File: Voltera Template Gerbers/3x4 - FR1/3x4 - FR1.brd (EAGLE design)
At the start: 135 x 101.6 mm, 1 part

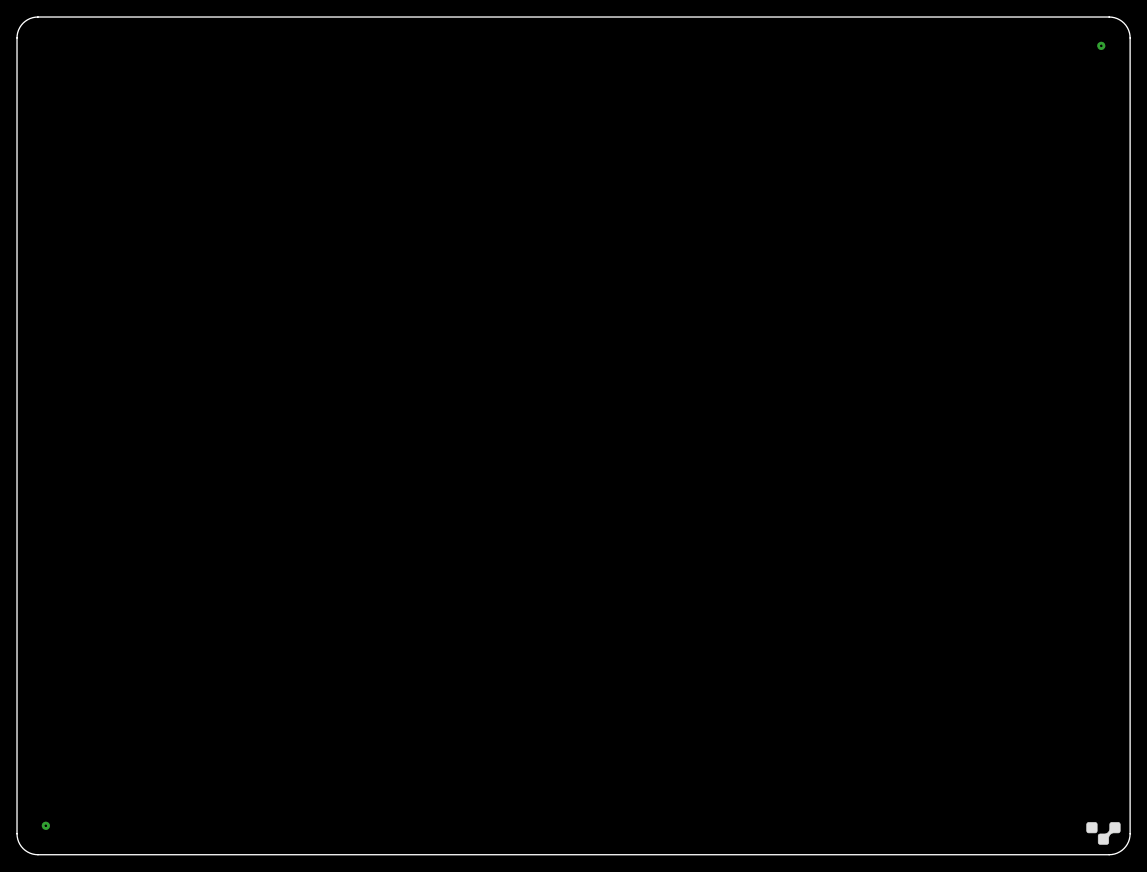
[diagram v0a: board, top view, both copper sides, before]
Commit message: Created 2x3 and 3x4 FR1 templates. Added 'fab' version of the templates
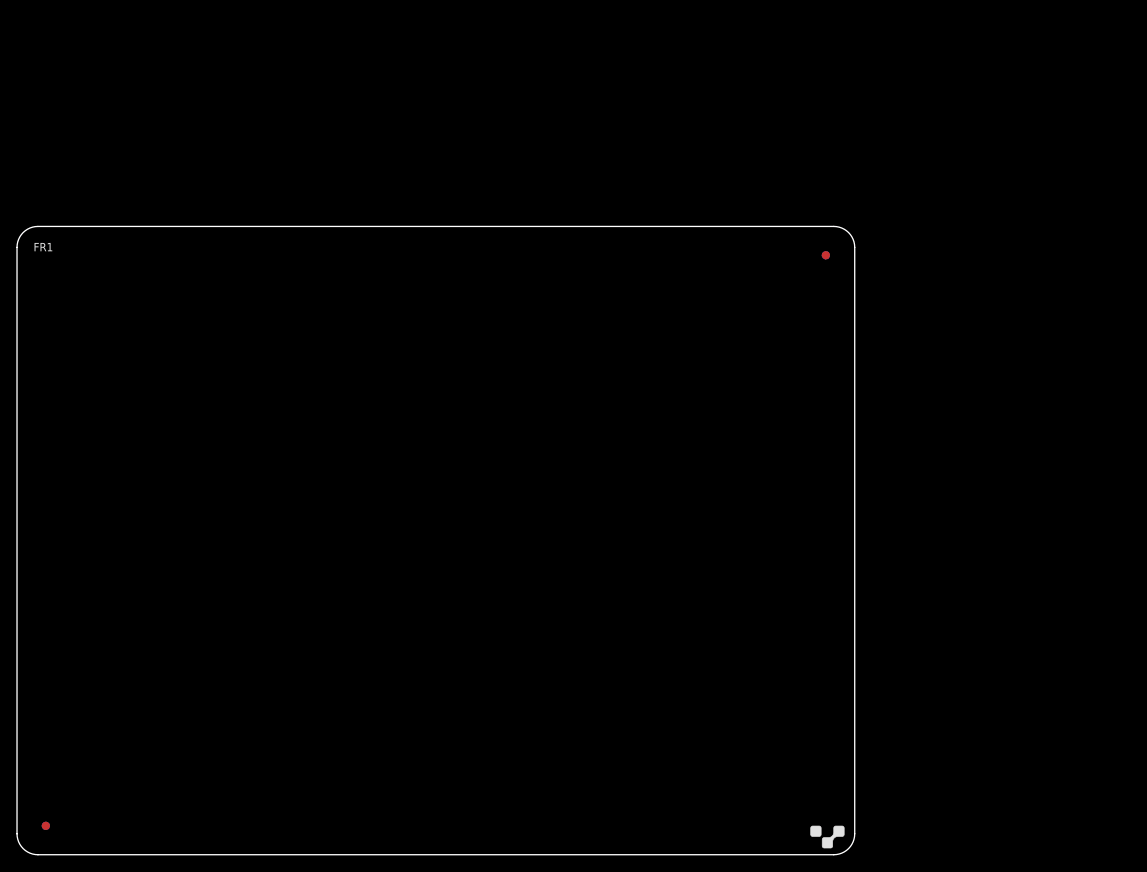
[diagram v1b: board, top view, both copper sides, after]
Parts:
- E$1: device voltera_community_lib:4X5_BOARD -> voltera_EAGLE_community_lib:3X4_BOARD_FR1
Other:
- board size 135 x 101.6 mm -> 101.6 x 76.2 mm
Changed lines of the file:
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@@
 <setting verticaltext="up"/>
 </settings>
-<grid distance="1" unitdist="mm" unit="mm" style="lines" multiple="1" display="yes" altdistance="0.1" altunitdist="mm" altunit="mm"/>
+<grid distance="0.05" unitdist="inch" unit="inch" style="lines" multiple="1" display="no" altdistance="0.025" altunitdist="inch" altunit="inch"/>
 <layers>
 <layer number="1" name="Top" color="4" fill="1" visible="yes" active="yes"/>
@@
 <layer number="27" name="tValues" color="7" fill="1" visible="yes" active="yes"/>
 <layer number="28" name="bValues" color="7" fill="1" visible="yes" active="yes"/>
-<layer number="29" name="tStop" color="7" fill="3" visible="no" active="yes"/>
-<layer number="30" name="bStop" color="7" fill="6" visible="no" active="yes"/>
-<layer number="31" name="tCream" color="7" fill="4" visible="no" active="yes"/>
-<layer number="32" name="bCream" color="7" fill="5" visible="no" active="yes"/>
-<layer number="33" name="tFinish" color="6" fill="3" visible="no" active="yes"/>
-<layer number="34" name="bFinish" color="6" fill="6" visible="no" active="yes"/>
-<layer number="35" name="tGlue" color="7" fill="4" visible="no" active="yes"/>
-<layer number="36" name="bGlue" color="7" fill="5" visible="no" active="yes"/>
-<layer number="37" name="tTest" color="7" fill="1" visible="no" active="yes"/>
-<layer number="38" name="bTest" color="7" fill="1" visible="no" active="yes"/>
+<layer number="29" name="tStop" color="7" fill="3" visible="yes" active="yes"/>
+<layer number="30" name="bStop" color="7" fill="6" visible="yes" active="yes"/>
+<layer number="31" name="tCream" color="7" fill="4" visible="yes" active="yes"/>
+<layer number="32" name="bCream" color="7" fill="5" visible="yes" active="yes"/>
+<layer number="33" name="tFinish" color="6" fill="3" visible="yes" active="yes"/>
+<layer number="34" name="bFinish" color="6" fill="6" visible="yes" active="yes"/>
+<layer number="35" name="tGlue" color="7" fill="4" visible="yes" active="yes"/>
+<layer number="36" name="bGlue" color="7" fill="5" visible="yes" active="yes"/>
+<layer number="37" name="tTest" color="7" fill="1" visible="yes" active="yes"/>
+<layer number="38" name="bTest" color="7" fill="1" visible="yes" active="yes"/>
 <layer number="39" name="tKeepout" color="4" fill="11" visible="yes" active="yes"/>
 <layer number="40" name="bKeepout" color="1" fill="11" visible="yes" active="yes"/>
@@
 <layer number="42" name="bRestrict" color="1" fill="10" visible="yes" active="yes"/>
 <layer number="43" name="vRestrict" color="2" fill="10" visible="yes" active="yes"/>
-<layer number="44" name="Drills" color="7" fill="1" visible="no" active="yes"/>
-<layer number="45" name="Holes" color="7" fill="1" visible="no" active="yes"/>
-<layer number="46" name="Milling" color="3" fill="1" visible="no" active="yes"/>
+<layer number="44" name="Drills" color="7" fill="1" visible="yes" active="yes"/>
+<layer number="45" name="Holes" color="7" fill="1" visible="yes" active="yes"/>
+<layer number="46" name="Milling" color="3" fill="1" visible="yes" active="yes"/>
 <layer number="47" name="Measures" color="7" fill="1" visible="yes" active="yes"/>
 <layer number="48" name="Document" color="7" fill="1" visible="yes" active="yes"/>
@@
 <board>
 <plain>
-<dimension x1="0" y1="3" x2="135" y2="3" x3="67.5" y3="-13" textsize="1.778" layer="47"/>
-<dimension x1="0" y1="0" x2="0" y2="101.6" x3="-4.8" y3="50.8" textsize="1.778" layer="47"/>
 </plain>
 <attributes>
@@
 </autorouter>
 <elements>
-<element name="E$1" library="voltera_community_lib" package="4X5_BOARD" value="" x="0" y="0"/>
+<element name="E$1" library="voltera_EAGLE_community_lib" package="3X4_BOARD_FR1" value="" x="0" y="0"/>
 </elements>
 <signals>
